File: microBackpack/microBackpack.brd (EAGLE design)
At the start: 121.9 x 76.2 mm, 75 parts, among them IC1 LM324D, IC2 LM324D, J2 USB_B_PTH, J4 2X6 FEMALE, U1 ATMEGA328P_TQFP, U2 5VREG-HS, U3 CP2102N-QFN24, U4 TVS_DIODE_4PK, U5 MCP4728, U6 78L09F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

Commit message: Did stuff
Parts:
- moved R26 118.8 mm to (22.1, 32.3), turned to 270 degrees
- moved R25 117.8 mm to (22.1, 36.3), turned to 270 degrees
- moved R38 19.3 mm to (5.59, 34.5), turned to 270 degrees
- moved R37 17.0 mm to (5.59, 38.6), turned to 270 degrees
- moved R27 16.2 mm to (3.30, 29.7)
- moved R28 16.2 mm to (3.30, 25.7)
- moved IC2 16.2 mm to (8.89, 26.9)
- moved U5 11.8 mm to (12.7, 35.6), turned to 0 degrees
- moved C11 11.0 mm to (3.30, 38.6), turned to 90 degrees
- moved C10 2.55 mm to (3.30, 34.5), turned to 270 degrees
- moved R18 0.25 mm to (19.8, 32.3)
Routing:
- net 12V: track 5.42 -> 72.0 mm, vias 0 -> 4
- net V_SET: track 3.02 -> 53.4 mm, vias 0 -> 2
- net I_SET: track 0.00 -> 32.7 mm
- net FGEN: track 7.75 -> 27.2 mm, vias 0 -> 2
- net I_OUT: track 6.65 -> 21.9 mm
- net N$12: track 0.00 -> 12.6 mm
- net N$4: track 0.00 -> 8.93 mm
- net GND: track 34.5 -> 35.8 mm, vias 18 -> 19

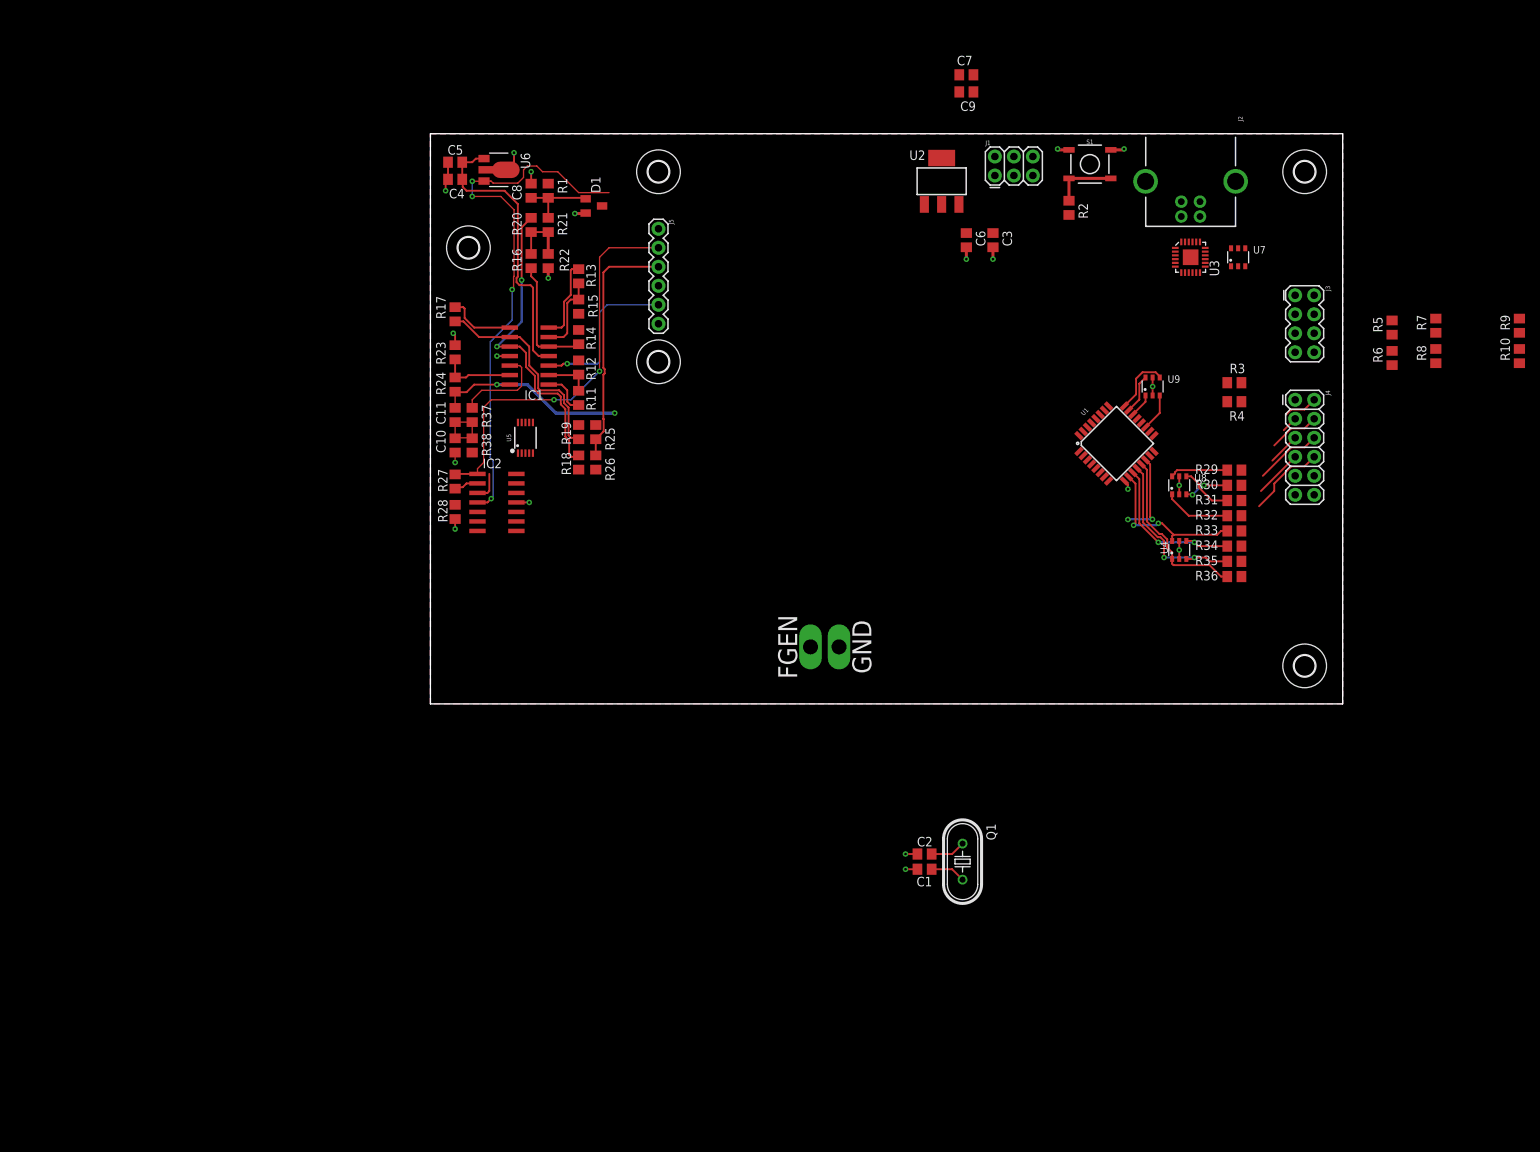
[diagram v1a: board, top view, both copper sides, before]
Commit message: Shrunk board to 3x3'' size
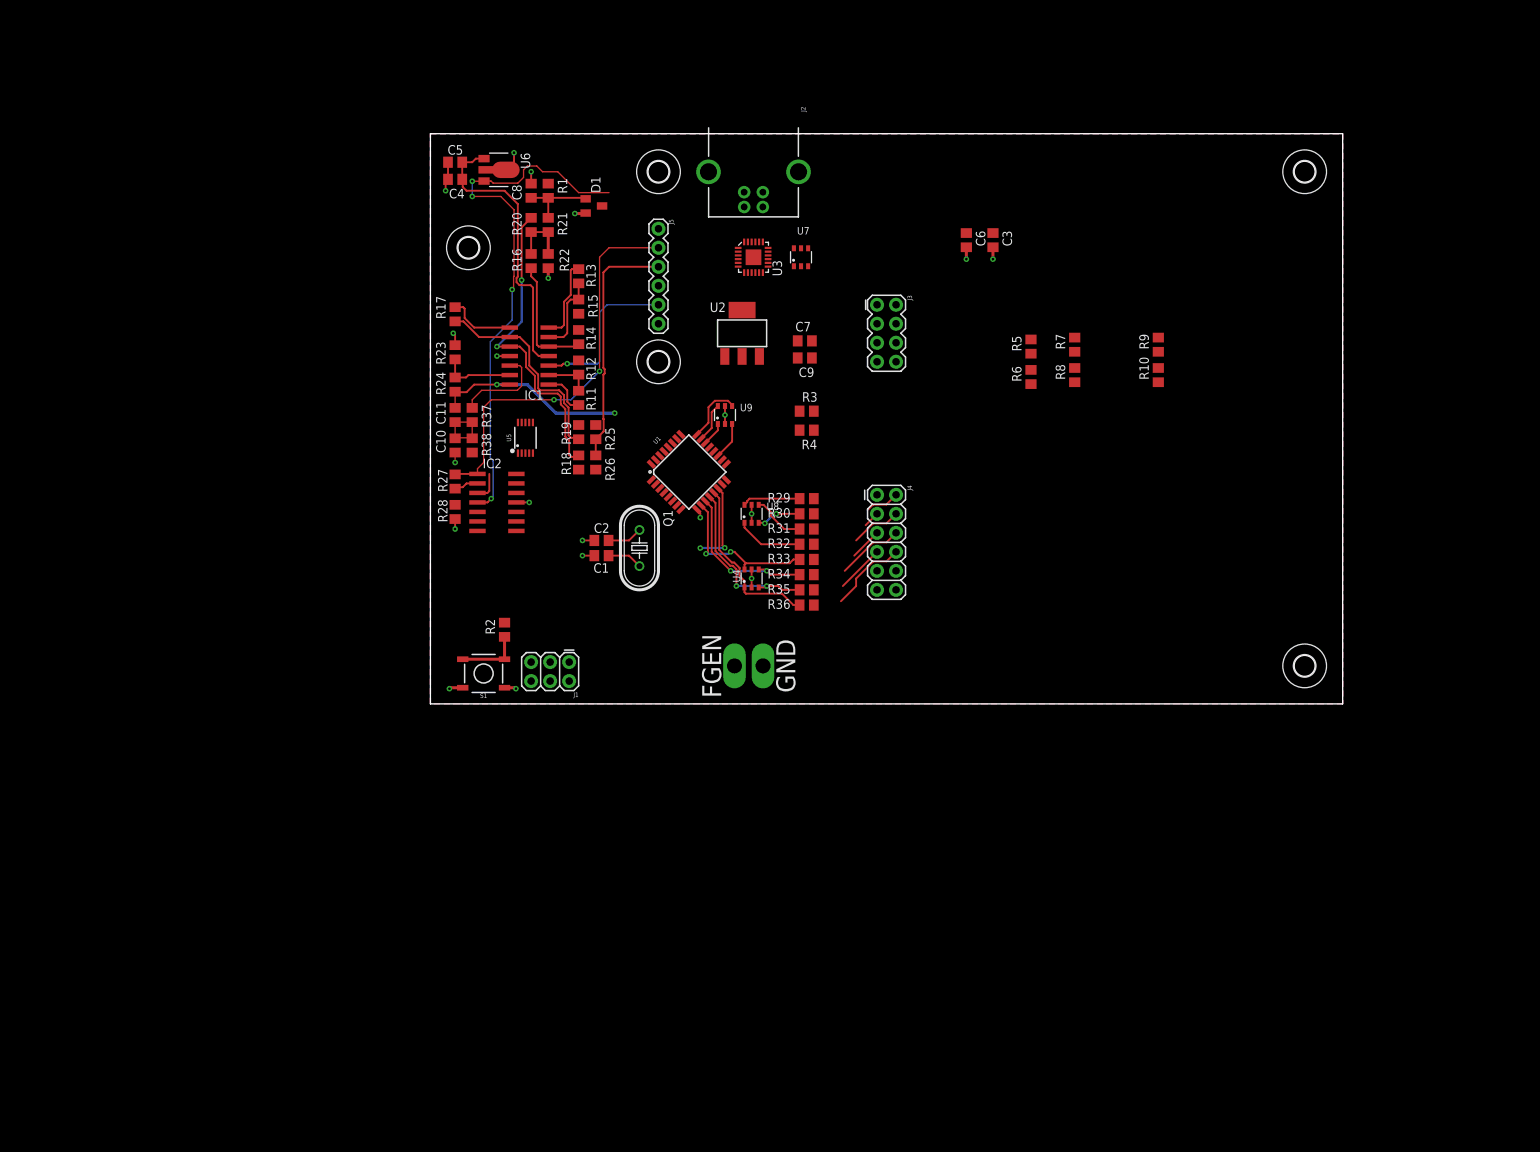
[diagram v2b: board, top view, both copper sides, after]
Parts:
- moved S1 105.8 mm to (7.11, 4.06), turned to 180 degrees
- moved R2 94.2 mm to (9.91, 9.91), turned to 90 degrees
- moved J1 86.4 mm to (18.5, 5.59), turned to 180 degrees
- moved C1 60.2 mm to (22.9, 19.8)
- moved C2 60.2 mm to (22.9, 21.8)
- moved Q1 60.2 mm to (27.9, 20.8)
- moved J2 58.4 mm to (43.2, 72.4)
- moved U7 58.4 mm to (49.5, 59.7)
- moved U3 58.4 mm to (43.2, 59.7)
- moved J4 57.3 mm to (59.7, 27.9)
- moved U1 57.3 mm to (34.5, 31.0)
- moved U9 57.3 mm to (39.4, 38.6)
- moved R29 57.3 mm to (50.3, 27.4)
- moved R3 57.3 mm to (50.3, 39.1)
- moved R30 57.3 mm to (50.3, 25.4)
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
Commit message: Added optoisolators to library. Wired up. Still need to finish USB power circuit.
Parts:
- added R39, R40: 10k, rcl:R0805
- added R41, R42, R43, R44: 100, rcl:R0603
- added R45: 1k, rcl:R0805
- added TP-RXLED, TP-TXLED, TP-USBGND, TP-USBVCC: TPPAD1-13, testpad:P1-13
- added U10, U11: TLP185, microBackpackLib:SO06-4
- moved H4 50.8 mm to (66.0, 5.08)
- moved H5 50.8 mm to (66.0, 71.1)
- moved C3 38.1 mm to (42.9, 41.7), turned to 180 degrees
- moved C6 33.2 mm to (42.9, 45.2), turned to 180 degrees
- moved U2 23.3 mm to (62.0, 38.1)
- moved FGEN 6.48 mm to (47.0, 6.35), turned to 180 degrees
- moved R10 4.02 mm to (93.5, 42.7)
- moved R5 4.02 mm to (76.5, 46.5)
- moved R6 4.02 mm to (76.5, 42.4)
- moved R9 4.02 mm to (93.5, 46.7)
- moved R7 4.02 mm to (82.3, 46.7)
- moved R8 4.02 mm to (82.3, 42.7)
- moved FGEN_GND 1.80 mm to (43.2, 6.35), turned to 180 degrees
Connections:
- new net N$13: R41.2, R42.1
- new net N$16: R39.2, U11.4, U3.20
- new net N$17: R43.2, R44.1
- new net N$18: R44.2, U10.3
- new net N$19: R41.1, U11.3
- new net N$20: R43.1, U3.21
- new net N$21: TP-RXLED.TP, U3.13
- new net N$22: TP-TXLED.TP, U3.14
- new net N$23: R45.1, U3.9
- new net USB_VCC: R45.2, TP-USBVCC.TP, U10.1, U11.6
- net GND: now also R40.1
- net MCU2USB: now also R42.2
- net USB2MCU: now also R40.2, U10.4
- net USB_GND: now also R39.1, TP-USBGND.TP
- net VCC: now also U10.6, U11.1
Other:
- board size 121.9 x 76.2 mm -> 71.1 x 76.2 mm

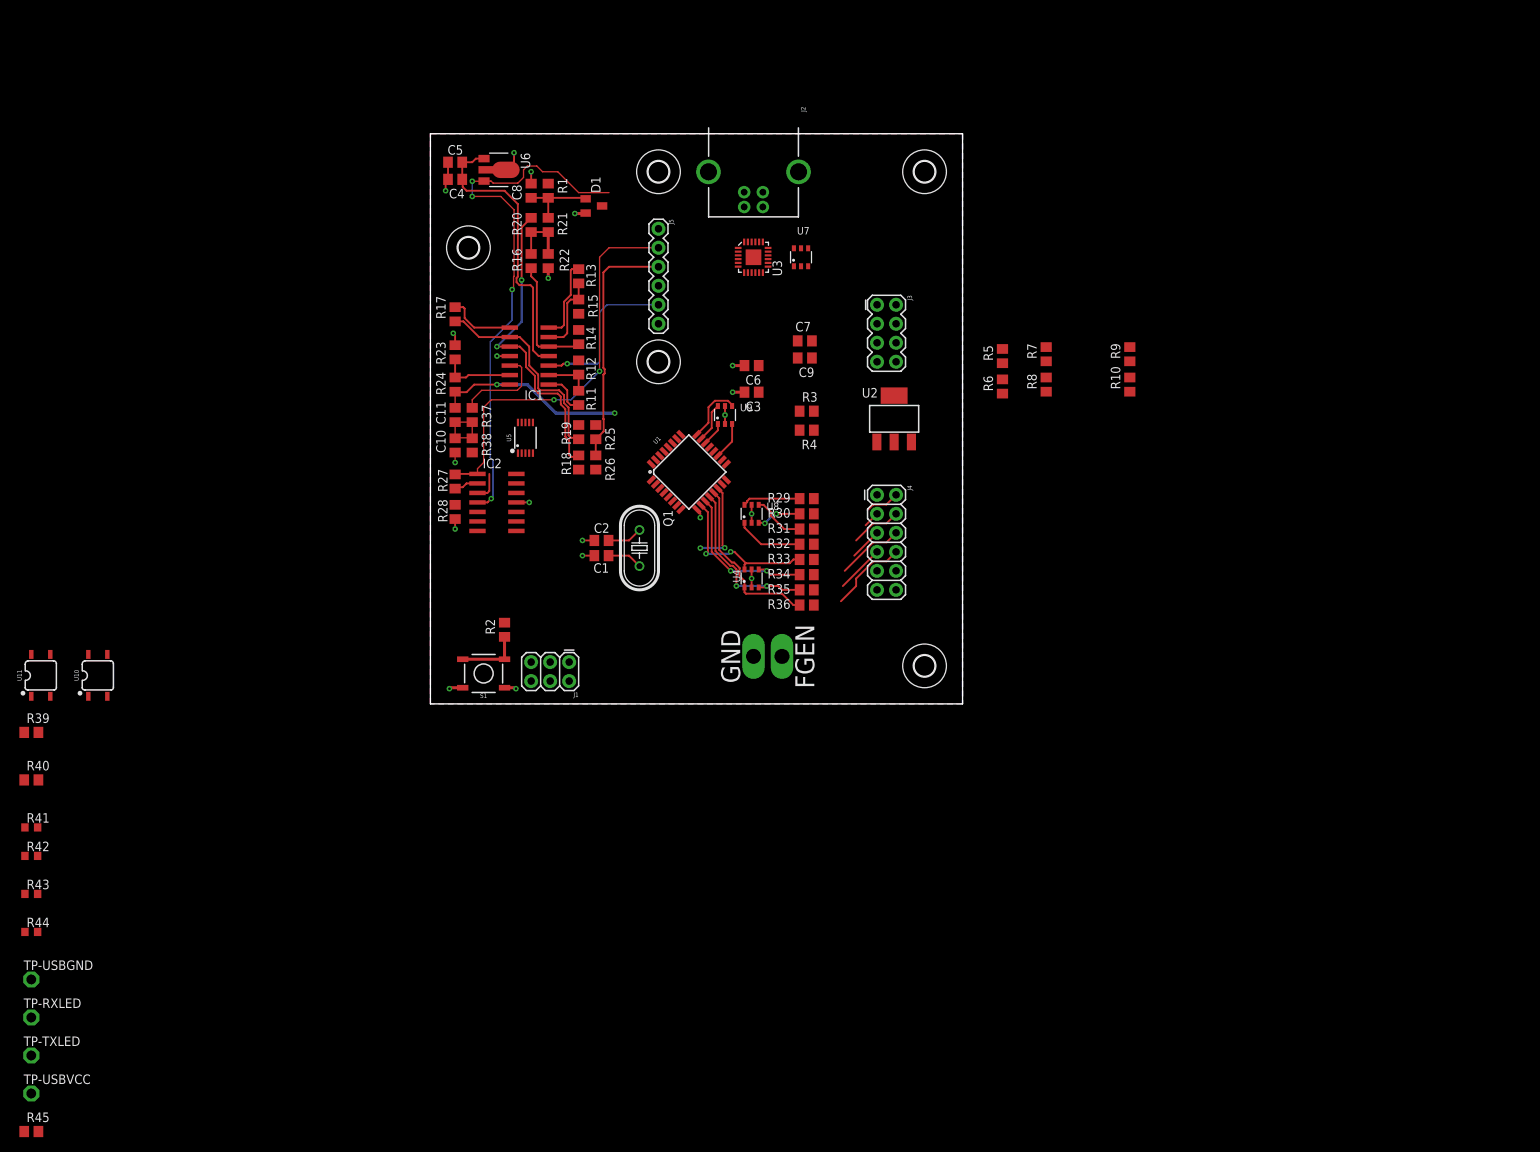
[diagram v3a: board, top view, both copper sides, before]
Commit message: Added usb power. Switched optocouplers to active-high
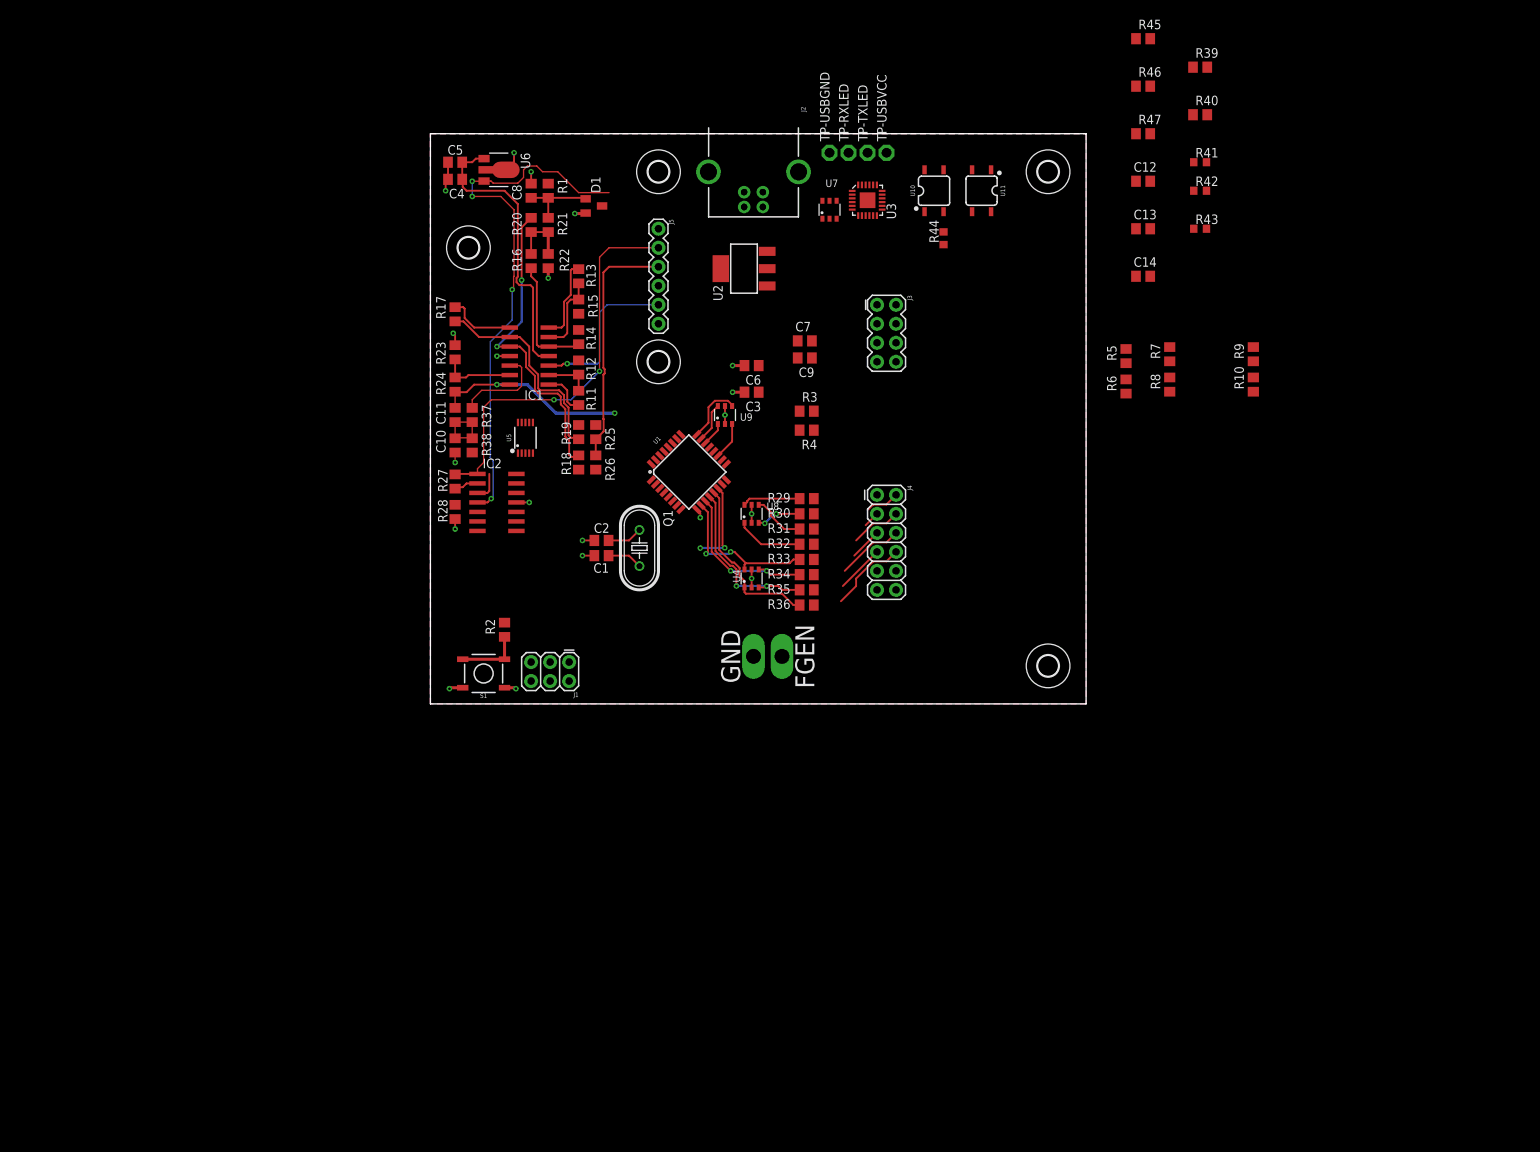
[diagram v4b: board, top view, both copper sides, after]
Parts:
- added C12, C13: 1uF, rcl:C0805
- added C14: 0.1uF, rcl:C0805
- added R46: 30.1k, rcl:R0805
- added R47: 15k, rcl:R0805
- moved R45 208.3 mm to (95.2, 88.9)
- moved R39 179.7 mm to (102.9, 85.1)
- moved R40 179.7 mm to (102.9, 78.7)
- moved R41 179.7 mm to (102.9, 72.4)
- moved R42 179.7 mm to (102.9, 68.6)
- moved R43 179.7 mm to (102.9, 63.5)
- moved TP-USBVCC 169.9 mm to (61.0, 73.7), turned to 90 degrees
- moved TP-TXLED 164.5 mm to (58.4, 73.7), turned to 90 degrees
- moved TP-RXLED 159.0 mm to (55.9, 73.7), turned to 90 degrees
- moved TP-USBGND 153.6 mm to (53.3, 73.7), turned to 90 degrees
- moved R44 153.2 mm to (68.6, 62.2), turned to 90 degrees
- moved U11 141.4 mm to (73.7, 68.6), turned to 180 degrees
- moved U10 129.2 mm to (67.3, 68.6)
- moved U2 28.4 mm to (41.9, 58.2), turned to 90 degrees
- moved U3 17.0 mm to (58.4, 67.3)
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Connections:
- removed net N$18: R44.2, U10.3
- removed net N$19: R41.1, U11.3
- new net D+: J2.D+, U3.3, U7.4
- new net D-: J2.D-, U3.4, U7.3
- new net VBUS: C12.1, J2.VBUS, R47.2, U3.7, U7.6
- net GND: now also U11.3
- net N$5: now also R41.1, U11.1; no longer J2.VBUS, U3.8
- net N$7: now also R46.2, R47.1, U3.8; no longer J2.D-, U3.4
- net N$8: now also R44.2, U10.1; no longer J2.D+, U3.3
- net USB_GND: now also C12.2, C13.2, C14.2, R46.1, U10.3, U3.EP
- net USB_VCC: now also C13.1, C14.1, U3.5, U3.6; no longer U10.1
- net VCC: no longer U11.1
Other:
- board size 71.1 x 76.2 mm -> 87.6 x 76.2 mm
